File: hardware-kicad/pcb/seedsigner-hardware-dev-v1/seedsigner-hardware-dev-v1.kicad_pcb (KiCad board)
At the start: 2 copper layers, 100 x 100 mm, 28 parts, among them J1 Conn_01x08_MountingPin, J2 Conn_01x08_MountingPin, SW1 SW_Push, SW2 SW_Push, SW3 SW_Push, SW4 SW_Push, SW5 SW_Push, SW6 SW_Push, SW7 SW_Push, SW8 SW_Push, U1 LuckFox_Pico_MINI, U2 WAVESHARE_LCD_BUTTON_BOARD_1.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, U3 RPI_ZERO

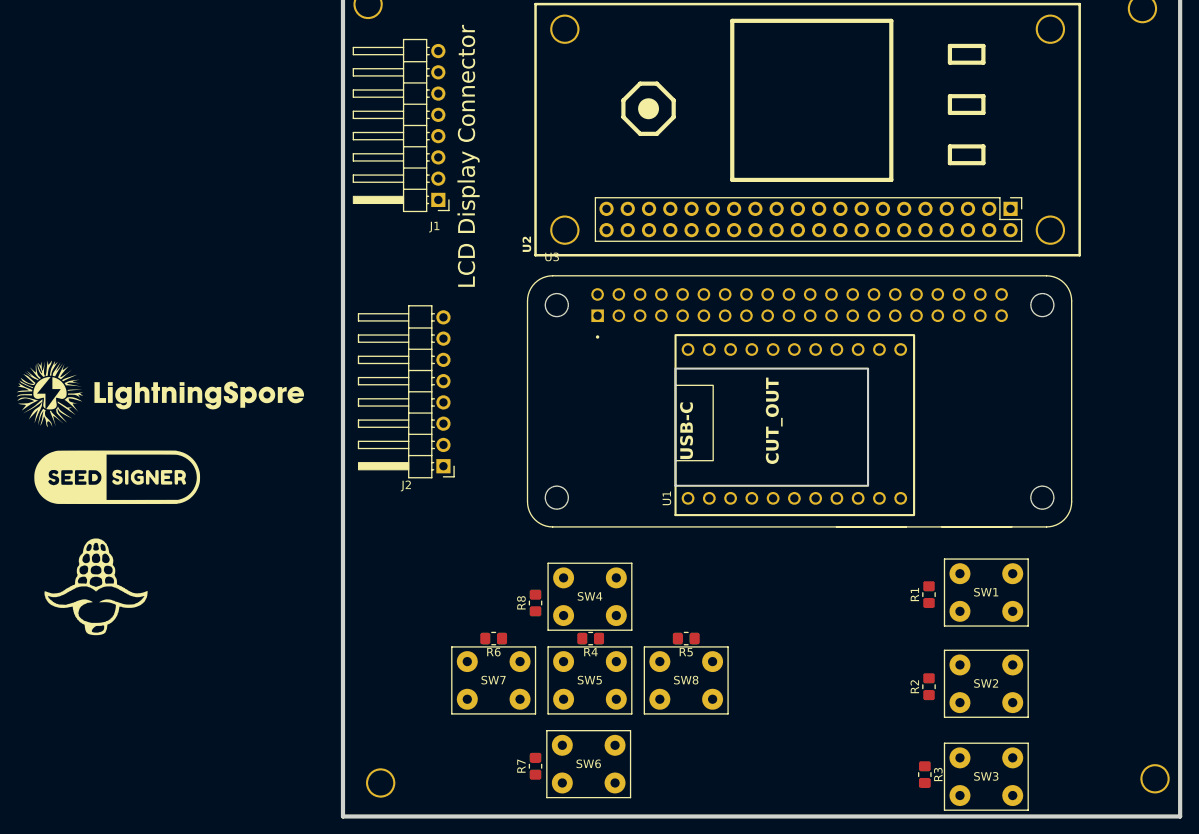
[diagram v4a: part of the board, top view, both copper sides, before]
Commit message: autoroute the hardware devboard
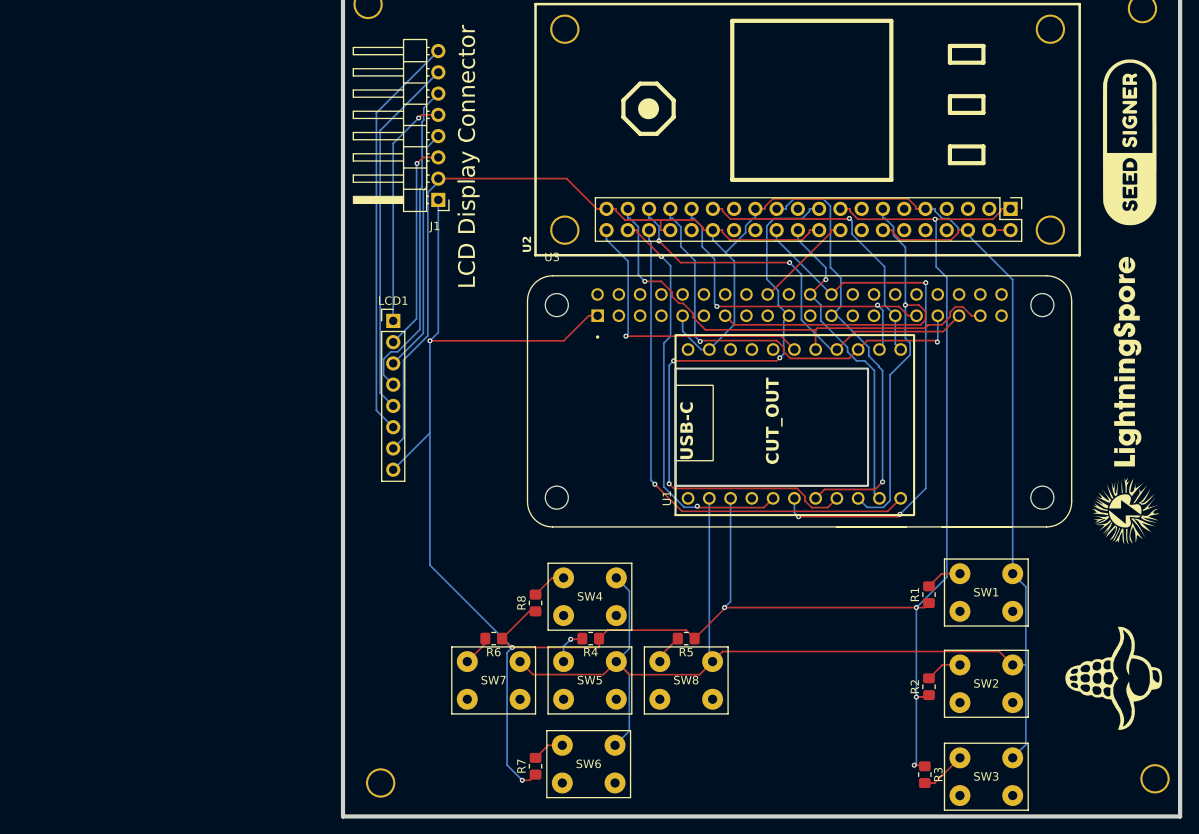
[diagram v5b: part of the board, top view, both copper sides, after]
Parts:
- removed J2: Conn_01x08_MountingPin, Connector_PinHeader_2.54mm:PinHeader_1x08_P2.54mm_Horizontal
- added LCD1: ST7789, Connector_PinHeader_2.54mm:PinHeader_1x08_P2.54mm_Vertical, F.Cu at (6.00, 40.8)
- moved LOGO1 127.4 mm to (94.0, 19.5), turned to 90 degrees
- moved LOGO2 122.0 mm to (92.0, 83.5), turned to 90 degrees
- moved ART1 115.0 mm to (93.5, 50.0), turned to 90 degrees
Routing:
- net GND: track 0.00 -> 328.7 mm
- net +3.3V: track 0.00 -> 270.0 mm, vias 0 -> 8
- net /Modules/SPI_MOSI: track 0.00 -> 74.3 mm, vias 0 -> 3
- net /Modules/RST: track 0.00 -> 70.3 mm, vias 0 -> 1
- net /Modules/SPI_CS: track 0.00 -> 65.8 mm, vias 0 -> 3
- net /Modules/KEY3: track 0.00 -> 62.0 mm, vias 0 -> 1
- net /Modules/JOYSTICK_RIGHT: track 0.00 -> 57.2 mm, vias 0 -> 1
- net /Modules/SPI_SCLK: track 0.00 -> 52.9 mm, vias 0 -> 1
- net /Modules/JOYSTICK_PRESS: track 0.00 -> 51.2 mm, vias 0 -> 2
- net /Modules/JOYSTICK_DOWN: track 0.00 -> 50.5 mm, vias 0 -> 2
- net /SPI_MOSI: track 0.00 -> 48.8 mm
- net /Modules/KEY2: track 0.00 -> 48.4 mm, vias 0 -> 2
- net /SPI_SCLK: track 0.00 -> 43.4 mm
- net /Modules/JOYSTICK_UP: track 0.00 -> 43.3 mm, vias 0 -> 2
- net /SPI_CS: track 0.00 -> 38.4 mm
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
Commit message: 2 different pcbs almost done
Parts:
- removed J1: Conn_01x08_MountingPin, Connector_PinHeader_2.54mm:PinHeader_1x08_P2.54mm_Horizontal
- removed U1: LuckFox_Pico_MINI, seedsigner-luckfox:LUCKFOX_PICO_MINI
- added C1: 0.1uF, Capacitor_SMD:C_0805_2012Metric_Pad1.18x1.45mm_HandSolder, F.Cu at (19.0, 79.0)
- added LCD2: ST7789, Connector_PinHeader_2.54mm:PinHeader_1x08_P2.54mm_Vertical, F.Cu at (5.00, 10.0)
- added R10: 10K, Resistor_SMD:R_0805_2012Metric_Pad1.20x1.40mm_HandSolder, F.Cu at (87.0, 46.0)
- added R11: 10K, Resistor_SMD:R_0805_2012Metric_Pad1.20x1.40mm_HandSolder, F.Cu at (5.00, 78.0)
- added R12: 10K, Resistor_SMD:R_0805_2012Metric_Pad1.20x1.40mm_HandSolder, F.Cu at (5.00, 81.0)
- added R13: 10K, Resistor_SMD:R_0805_2012Metric_Pad1.20x1.40mm_HandSolder, F.Cu at (5.00, 76.0)
- added R14: 10K, Resistor_SMD:R_0805_2012Metric_Pad1.20x1.40mm_HandSolder, F.Cu at (5.00, 74.0)
- added R9: 10K, Resistor_SMD:R_0805_2012Metric_Pad1.20x1.40mm_HandSolder, F.Cu at (87.0, 43.0)
- added TP1: TestPoint, TestPoint:TestPoint_Pad_D1.0mm, F.Cu at (11.0, 96.0)
- added TP2: TestPoint, TestPoint:TestPoint_Pad_D1.0mm, F.Cu at (14.0, 96.0)
- added TP3: TestPoint, TestPoint:TestPoint_Pad_D1.0mm, F.Cu at (17.0, 96.0)
- added TP4: TestPoint, TestPoint:TestPoint_Pad_D1.0mm, F.Cu at (20.0, 96.0)
- added TP5: TestPoint, TestPoint:TestPoint_Pad_D1.0mm, F.Cu at (22.5, 96.0)
- added TP6: TestPoint, TestPoint:TestPoint_Pad_D1.0mm, F.Cu at (25.0, 96.0)
- added U4: LuckFox_Pico_PLUS_PRO, seedsigner-luckfox:LUCKFOX_PICO, F.Cu at (51.0, 53.0)
- added U5: PCA9539PW_112, seedsigner-luckfox:SOP65P640X110-24N, F.Cu at (13.0, 80.0)
- moved LCD1 19.2 mm to (5.00, 60.0), turned to 180 degrees
- moved R6 11.0 mm to (29.0, 78.0)
- moved SW7 11.0 mm to (29.0, 83.0)
- moved SW6 10.8 mm to (40.0, 92.0)
- moved SW4 10.5 mm to (40.0, 73.0)
- moved SW5 10.5 mm to (40.0, 83.0)
- moved R4 10.4 mm to (40.0, 78.0)
- moved R7 10.2 mm to (33.0, 92.0)
- moved R8 10.1 mm to (33.0, 73.0)
- moved R5 10.0 mm to (51.0, 78.0)
- moved SW8 10.0 mm to (51.0, 83.0)
- moved SW3 7.58 mm to (70.0, 92.0)
- moved R2 7.16 mm to (63.0, 83.0)
- moved R3 7.16 mm to (63.0, 92.0), turned to 90 degrees
- moved R1 7.02 mm to (63.0, 73.0)
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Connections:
- LCD1 pad 1: /BACKLIGHT -> BACKLIGHT_PWM
- LCD1 pad 2: /RST -> LCD_RST
- LCD1 pad 3: /DC -> LCD_DC
- LCD1 pad 4: /SPI_CS -> SPI_CS
- LCD1 pad 5: /SPI_SCLK -> SPI_SCLK
- LCD1 pad 6: /SPI_MOSI -> SPI_MOSI
- R1 pad 2: /Buttons/KEY1 -> KEY1
- R2 pad 2: /Buttons/KEY2 -> KEY2
- R3 pad 2: /Buttons/KEY3 -> KEY3
- R4 pad 2: /Buttons/JOYSTICK_RIGHT -> JOYSTICK_RIGHT
- R5 pad 2: /Buttons/JOYSTICK_PRESS -> JOYSTICK_PRESS
- R6 pad 2: /Buttons/JOYSTICK_DOWN -> JOYSTICK_DOWN
- R7 pad 2: /Buttons/JOYSTICK_UP -> JOYSTICK_UP
- R8 pad 2: /Buttons/JOYSTICK_LEFT -> JOYSTICK_LEFT
- SW1 pad 1: /Buttons/KEY1 -> KEY1
- SW2 pad 1: /Buttons/KEY2 -> KEY2
- SW3 pad 1: /Buttons/KEY3 -> KEY3
- SW4 pad 1: /Buttons/JOYSTICK_LEFT -> JOYSTICK_LEFT
- SW5 pad 1: /Buttons/JOYSTICK_RIGHT -> JOYSTICK_RIGHT
- SW6 pad 1: /Buttons/JOYSTICK_UP -> JOYSTICK_UP
- SW7 pad 1: /Buttons/JOYSTICK_DOWN -> JOYSTICK_DOWN
- SW8 pad 1: /Buttons/JOYSTICK_PRESS -> JOYSTICK_PRESS
- U2 pad 13: /Modules/RST -> LCD_RST
- U2 pad 18: /Modules/BACKLIGHT -> BACKLIGHT_PWM
- U2 pad 19: /Modules/SPI_MOSI -> SPI_MOSI
- U2 pad 22: /Modules/DC -> LCD_DC
- U2 pad 23: /Modules/SPI_SCLK -> SPI_SCLK
- U2 pad 24: /Modules/SPI_CS -> SPI_CS
- U2 pad 29: /Modules/JOYSTICK_LEFT -> JOYSTICK_LEFT
- U2 pad 31: /Modules/JOYSTICK_UP -> JOYSTICK_UP
- U2 pad 33: /Modules/JOYSTICK_PRESS -> JOYSTICK_PRESS
- U2 pad 35: /Modules/JOYSTICK_DOWN -> JOYSTICK_DOWN
- U2 pad 36: /Modules/KEY3 -> KEY3
- U2 pad 37: /Modules/JOYSTICK_RIGHT -> JOYSTICK_RIGHT
- U2 pad 38: /Modules/KEY2 -> KEY2
- U2 pad 40: /Modules/KEY1 -> KEY1
- U3 pad 13: /Modules/RST -> LCD_RST
- U3 pad 18: /Modules/BACKLIGHT -> BACKLIGHT_PWM
- U3 pad 19: /Modules/SPI_MOSI -> SPI_MOSI
- U3 pad 22: /Modules/DC -> LCD_DC
- U3 pad 23: /Modules/SPI_SCLK -> SPI_SCLK
- U3 pad 24: /Modules/SPI_CS -> SPI_CS
- U3 pad 29: /Modules/JOYSTICK_LEFT -> JOYSTICK_LEFT
- U3 pad 3: unconnected-(U3-GPIO2_SDA-Pad3) -> I2C_SDA
- U3 pad 31: /Modules/JOYSTICK_UP -> JOYSTICK_UP
- U3 pad 33: /Modules/JOYSTICK_PRESS -> JOYSTICK_PRESS
- U3 pad 35: /Modules/JOYSTICK_DOWN -> JOYSTICK_DOWN
- U3 pad 37: /Modules/JOYSTICK_RIGHT -> JOYSTICK_RIGHT
- U3 pad 5: unconnected-(U3-GPIO3_SCL-Pad5) -> I2C_SCL
- U3 pad 7: unconnected-(U3-GPIO4_GPCKL0-Pad7) -> IO_INT
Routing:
- net LCD_RST: track 0.00 -> 195.9 mm, vias 0 -> 2
- net JOYSTICK_RIGHT: track 0.00 -> 172.5 mm, vias 0 -> 1
- net LCD_DC: track 0.00 -> 165.3 mm, vias 0 -> 1
- net BACKLIGHT_PWM: track 0.00 -> 162.2 mm, vias 0 -> 1
- net JOYSTICK_PRESS: track 0.00 -> 159.3 mm, vias 0 -> 2
- net JOYSTICK_DOWN: track 0.00 -> 148.8 mm, vias 0 -> 3
- net JOYSTICK_LEFT: track 0.00 -> 133.8 mm, vias 0 -> 1
- net KEY1: track 0.00 -> 133.3 mm, vias 0 -> 2
- net KEY3: track 0.00 -> 131.2 mm, vias 0 -> 2
- net JOYSTICK_UP: track 0.00 -> 130.7 mm, vias 0 -> 2
- net KEY2: track 0.00 -> 128.1 mm, vias 0 -> 1
- net SPI_CS: track 0.00 -> 125.4 mm, vias 0 -> 2
- net SPI_MOSI: track 0.00 -> 124.4 mm, vias 0 -> 1
- net GND: track 328.7 -> 206.5 mm, vias 0 -> 2
- net I2C_SCL: track 0.00 -> 120.0 mm, vias 0 -> 1
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- added copper zone on B.Cu, net GND
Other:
- board text added: "GND VCC"
- board text added: "KEY1"
- board text added: "KEY2"
- board text added: "KEY3"
- board text added: "PWM RST DC CS SCLK MOSI GND VCC"

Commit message: close to ordering on jlcpcb
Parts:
- moved R10 9.28 mm to (78.0, 48.2), turned to -90 degrees
- moved R9 7.97 mm to (81.0, 48.2), turned to -90 degrees
- moved ART1 1.77 mm to (93.8, 51.8)
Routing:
- net GND: track 206.5 -> 183.9 mm
- net I2C_SCL: track 120.0 -> 109.5 mm
- net I2C_SDA: track 115.3 -> 105.8 mm
- net +3.3V: track 357.4 -> 354.4 mm
- net LCD_RST: track 195.9 -> 198.4 mm
- net JOYSTICK_UP: track 130.7 -> 129.5 mm
- net JOYSTICK_PRESS: track 159.3 -> 160.1 mm
- net SPI_MOSI: track 124.4 -> 123.7 mm

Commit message: pcb checkin, ordered
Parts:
- added ART2: Modulo, seedsigner-luckfox:modulo-1, F.Cu at (94.0, 83.0)
- added J1: Conn_01x04, Connector:NS-Tech_Grove_1x04_P2mm_Vertical, F.Cu at (5.00, 84.0)
- added TP10: TestPoint, TestPoint:TestPoint_Pad_D1.0mm, F.Cu at (30.0, 96.0)
- added TP7: TestPoint, TestPoint:TestPoint_Pad_D1.0mm, F.Cu at (27.0, 96.0)
- added TP8: TestPoint, TestPoint:TestPoint_Pad_D1.0mm, F.Cu at (34.0, 96.0)
- added TP9: TestPoint, TestPoint:TestPoint_Pad_D1.0mm, F.Cu at (23.0, 96.0)
- moved LOGO2 80.8 mm to (50.0, 15.0), turned to 0 degrees
- moved TP6 7.00 mm to (32.0, 96.0)
- moved R12 3.00 mm to (5.00, 78.0)
- moved TP5 2.50 mm to (25.0, 96.0)
- moved R11 2.00 mm to (5.00, 76.0)
- moved R13 2.00 mm to (5.00, 74.0)
- moved R14 2.00 mm to (5.00, 72.0)
- moved ART1 0.35 mm to (94.0, 52.0)
- moved R10 0.25 mm to (78.0, 48.0)
- moved R9 0.25 mm to (81.0, 48.0)
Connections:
- R11 pad 2: Net-(U5-~RESET) -> IO_RST
- U3 pad 30: unconnected-(U3-GND_6-Pad30) -> IO_RST
- U3 pad 34: unconnected-(U3-GND_7-Pad34) -> GND
- U4 pad 21: unconnected-(U4-GPIO2_A4_d-Pad21) -> IO_RST
- U4 pad 23: unconnected-(U4-GND-Pad23) -> GND
- U5 pad 3: Net-(U5-~RESET) -> IO_RST
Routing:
- net IO_RST: track 0.00 -> 128.4 mm, vias 0 -> 4
- net GND: track 183.9 -> 98.5 mm, vias 2 -> 4
- net I2C_SCL: track 109.5 -> 160.9 mm, vias 1 -> 2
- net I2C_SDA: track 105.8 -> 155.7 mm, vias 1 -> 2
- net +3.3V: track 354.4 -> 373.6 mm
- net IO_INT: track 106.8 -> 99.1 mm
- net Net-(U5-~RESET): track 4.20 -> 0.00 mm
- net JOYSTICK_RIGHT: track 172.9 -> 175.4 mm
- net Net-(U5-A1): track 4.53 -> 6.41 mm
- net JOYSTICK_UP: track 129.5 -> 128.0 mm
- net KEY1: track 133.3 -> 134.5 mm, vias 2 -> 4
- net SPI_CS: track 125.6 -> 124.6 mm
- net JOYSTICK_LEFT: track 133.8 -> 134.6 mm
- net Net-(U5-A0): track 11.1 -> 11.8 mm
- net KEY2: track 128.1 -> 128.7 mm
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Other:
- board text added: "Hardware DevBoard V1"
- board text removed: "SeedSigner Hardware DevBoard"
